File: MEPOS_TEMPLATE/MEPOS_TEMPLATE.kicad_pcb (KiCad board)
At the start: 4 copper layers, 101.6 x 101.6 mm, 9 parts, among them J201 Conn_02x32_Odd_Even, J202 Conn_02x20_Odd_Even

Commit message: Updated to MEPOS V0.5
-updated pinout so pin names matched schematic.
-added paste holes for alignment
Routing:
- added copper zone on In2.Cu, net GND
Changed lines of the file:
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@@
   (title_block
     (title "MEPOS Template")
-    (date "2022-04-24")
-    (rev "V22.04.0.4")
+    (date "2022-05-15")
+    (rev "V22.04.0.5")
   )
   (layers
     (0 "F.Cu" signal)
-    (1 "In1.Cu" power "GND.Cu")
-    (2 "In2.Cu" power "Power.Cu")
+    (1 "In1.Cu" power "GND1.Cu")
+    (2 "In2.Cu" power "GND2.Cu")
     (31 "B.Cu" signal)
     (32 "B.Adhes" user "B.Adhesive")
@@
   (gr_circle locked (center 192.545 68.885) (end 193.18 68.885) (layer "B.Cu") (width 0.001) (fill solid))
   (gr_circle locked (center 191.275 66.345) (end 191.91 66.345) (layer "B.Cu") (width 0.001) (fill solid))
+  (gr_circle (center 190.64 130.48) (end 192.24 130.48) (layer "B.Paste") (width 0.001) (fill solid))
+  (gr_circle (center 99.2 130.48) (end 100.8 130.48) (layer "B.Paste") (width 0.001) (fill solid))
+  (gr_circle (center 190.64 39.04) (end 192.24 39.04) (layer "B.Paste") (width 0.001) (fill solid))
+  (gr_circle (center 99.2 39.04) (end 100.8 39.04) (layer "B.Paste") (width 0.001) (fill solid))
+  (gr_circle (center 99.2 130.48) (end 100.8 130.48) (layer "F.Paste") (width 0.001) (fill solid))
+  (gr_circle (center 190.64 39.04) (end 192.24 39.04) (layer "F.Paste") (width 0.001) (fill solid))
+  (gr_circle (center 99.2 39.04) (end 100.8 39.04) (layer "F.Paste") (width 0.001) (fill solid))
+  (gr_circle (center 190.64 130.48) (end 192.24 130.48) (layer "F.Paste") (width 0.001) (fill solid))
   (gr_line locked (start 180.48 77.14) (end 195.72 77.14) (layer "B.SilkS") (width 0.12))
   (gr_line locked (start 195.72 84.76) (end 180.48 84.76) (layer "B.SilkS") (width 0.12))
@@
   (segment locked (start 100.47 47.93) (end 103.01 47.93) (width 1.27) (layer "F.Cu") (net 54))
   (segment locked (start 100.47 45.39) (end 103.01 45.39) (width 1.27) (layer "F.Cu") (net 55))
-  (zone locked (net 1) (net_name "GND") (layer "In1.Cu") (hatch edge 0.508)
-    (connect_pads (clearance 0.508))
+  (zone locked (net 1) (net_name "GND") (layers "In1.Cu" "In2.Cu") (hatch edge 0.508)
+    (connect_pads yes (clearance 0.508))
     (min_thickness 0.254) (filled_areas_thickness no)
-    (fill yes (thermal_gap 0.508) (thermal_bridge_width 0.508))
+    (fill yes (thermal_gap 0.508) (thermal_bridge_width 0.508) (smoothing fillet) (radius 1))
     (polygon
       (pts

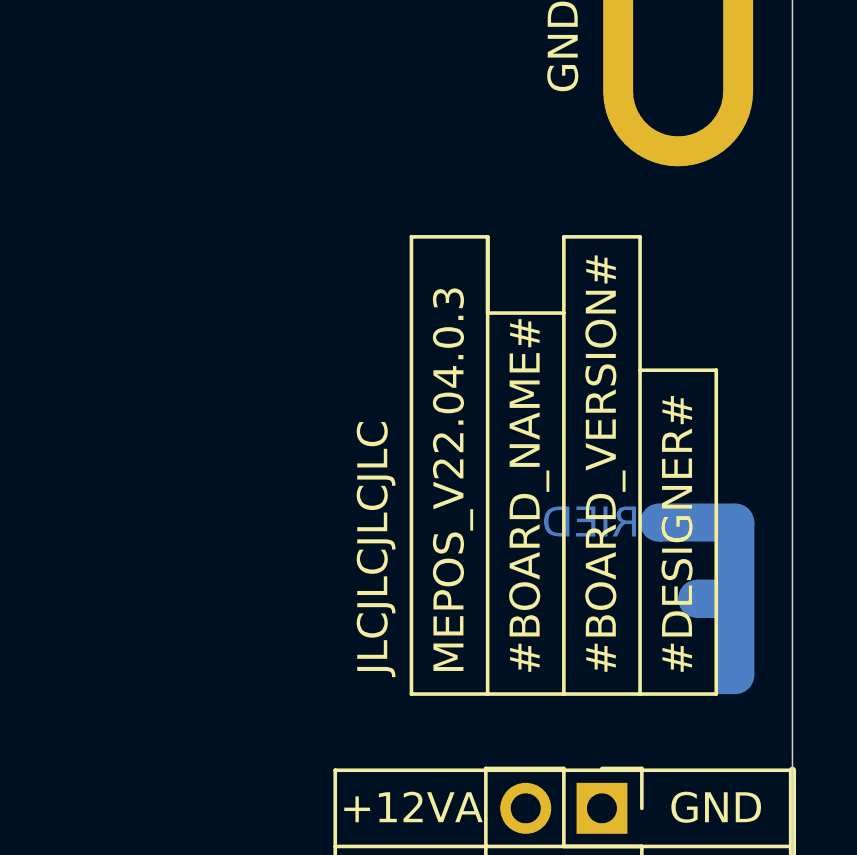
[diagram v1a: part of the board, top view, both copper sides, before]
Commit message: Updated Silkscreen version error
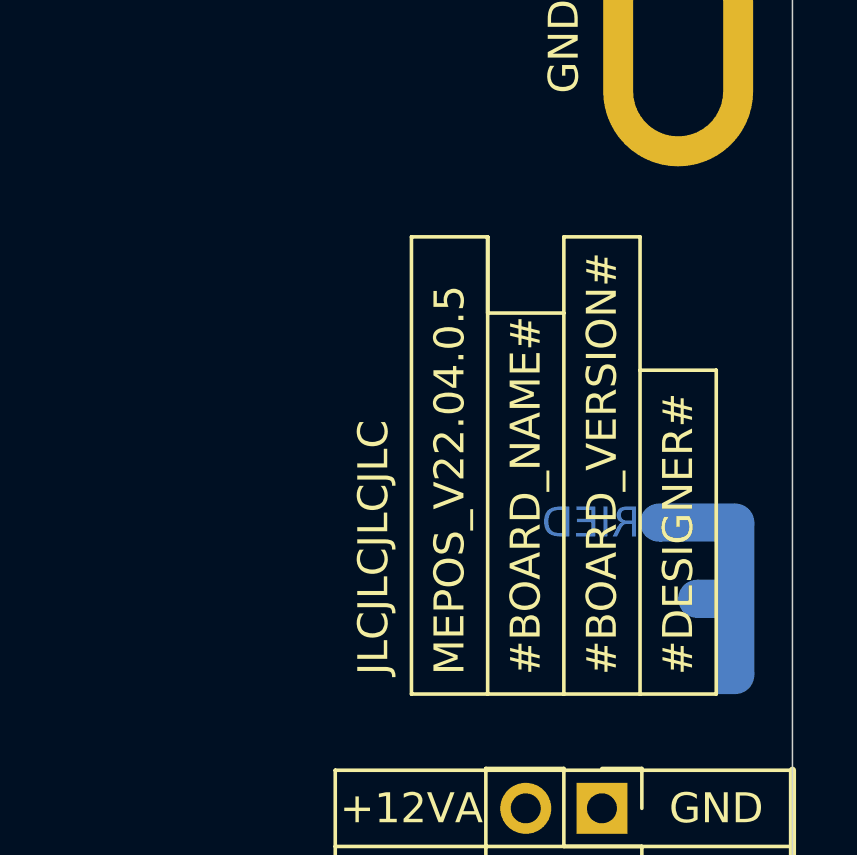
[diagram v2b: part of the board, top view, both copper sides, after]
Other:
- board text added: "MEPOS_V22.04.0.5"
- board text removed: "MEPOS_V22.04.0.3"
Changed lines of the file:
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@@
   (gr_circle (center 99.2 130.48) (end 100.8 130.48) (layer "F.Paste") (width 0.001) (fill solid))
   (gr_circle (center 190.64 39.04) (end 192.24 39.04) (layer "F.Paste") (width 0.001) (fill solid))
+  (gr_circle (center 190.64 130.48) (end 192.24 130.48) (layer "F.Paste") (width 0.001) (fill solid))
   (gr_circle (center 99.2 39.04) (end 100.8 39.04) (layer "F.Paste") (width 0.001) (fill solid))
-  (gr_circle (center 190.64 130.48) (end 192.24 130.48) (layer "F.Paste") (width 0.001) (fill solid))
   (gr_line locked (start 180.48 77.14) (end 195.72 77.14) (layer "B.SilkS") (width 0.12))
   (gr_line locked (start 195.72 84.76) (end 180.48 84.76) (layer "B.SilkS") (width 0.12))
@@
     (effects (font (size 1 1) (thickness 0.15)))
   )
-  (gr_text "MEPOS_V22.04.0.3" (at 184.29 71.425 90) (layer "F.SilkS")
+  (gr_text "MEPOS_V22.04.0.5" (at 184.29 71.425 90) (layer "F.SilkS")
     (effects (font (size 1 1) (thickness 0.15)) (justify left))
   )
